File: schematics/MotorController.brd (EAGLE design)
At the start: 160 x 100 mm, 30 parts, among them K1 35701331

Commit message: no message
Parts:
- removed POWER-INPUT: 1, con-lstb:MA03-1
- added DC_MOTOR_DRIVER: SINGLE_MOTOR_DRIVER, pololu motor driver:MOTOR_DRIVER_MC33926_FOOTPRINT_
- added IC1: (no value), v-reg:78XXL
- added LED1: (no value), led:LED3MM
- added LOG-UART: 1, con-lstb:MA03-1
- added POWER_IN: (no value), SparkFun-Connectors:SCREWTERMINAL-3.5MM-2
- added R11: 1K, resistor:0204/5
- D1: value 1N4148DO35-7 -> 1N5400; device diode:DO35-7 -> diode:DO201-15
- MOTOR1, MOTOR2, MOTOR3: value 1 -> 5566-4; device con-lstb:MA03-1 -> con-molex:5566-4
- moved C3 285.2 mm to (44.5, 82.5), turned to 180 degrees
- moved C2 280.7 mm to (124.5, 68.6), turned to 180 degrees
- moved C1 271.8 mm to (116.8, 80.0), turned to 180 degrees
- moved CONTROL-I2C 241.9 mm to (88.9, 86.4), turned to 180 degrees
- moved D1 238.7 mm to (118.1, 53.3)
- moved IMU-I2C 227.0 mm to (63.5, 86.4)
- moved K1 205.4 mm to (138.4, 71.1), turned to 90 degrees
- moved DC-MOTOR 201.4 mm to (127.0, 12.7)
- moved R10 190.6 mm to (100.3, 58.4), turned to 180 degrees
- moved T1 188.1 mm to (106.7, 55.9), turned to 90 degrees
- moved ENCODER1 159.9 mm to (106.7, 12.7), turned to 270 degrees
- moved ENCODER2 159.1 mm to (82.5, 12.7), turned to 270 degrees
- moved R9 155.2 mm to (61.0, 55.9), turned to 270 degrees
- moved R8 151.4 mm to (63.5, 55.9), turned to 270 degrees
- moved R7 147.8 mm to (66.0, 55.9), turned to 270 degrees
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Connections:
- removed net GND: C1.-, C2.-, C3.2, CONTROL-I2C.3, DC-MOTOR.4, DRK1.GND, DRK2.GND, DRK3.GND, ENCODER1.4, ENCODER2.4, ENCODER3.4, IMU-I2C.3, POWER-INPUT.1, PRJ1.GND, T1.1
- removed net VCC: C1.+, C3.1, D1.C, DC-MOTOR.3, ENCODER1.1, ENCODER2.1, ENCODER3.1, K1.3, PRJ1.VIN
- new net BLCK-M2: DC-MOTOR.2, DC_MOTOR_DRIVER.OUT1
- new net ENC_B: DC-MOTOR.6, PRJ1.35/A16
- new net ENC_GND: C1.-, C2.-, C3.2, CONTROL-I2C.3, DC-MOTOR.3, DC_MOTOR_DRIVER.GND, DRK1.GND, DRK2.GND, DRK3.GND, ENCODER1.4, ENCODER2.4, ENCODER3.4, IC1.GND, IMU-I2C.3, LED1.A, LOG-UART.3, POWER_IN.1, PRJ1.GND, T1.1
- new net ENC_VCC: C1.+, C3.1, DC-MOTOR.4, DC_MOTOR_DRIVER.VIN, ENCODER1.1, ENCODER2.1, ENCODER3.1, IC1.OUT, K1.3, PRJ1.VIN, R11.2
- new net N$44: DC_MOTOR_DRIVER.IN1, PRJ1.29
- new net N$45: DC_MOTOR_DRIVER.EN, PRJ1.31/A12
- new net N$46: PRJ1.36/A17
- new net N$47: DC_MOTOR_DRIVER.IN2, PRJ1.30
- new net RED-M1: DC-MOTOR.1, DC_MOTOR_DRIVER.OUT2
- new net RX5: LOG-UART.1, PRJ1.34/A15
- new net TX5: LOG-UART.2, PRJ1.33/A14
- net N$12: now also DC_MOTOR_DRIVER.VIN(5-28V)
- net N$32: now also D1.A, IC1.IN, POWER_IN.2; no longer K1.7, POWER-INPUT.3
- net N$39: now also D1.C, K1.7; no longer D1.A, POWER-INPUT.2
- net N$40: now also LED1.K, R11.1; no longer DC-MOTOR.2, PRJ1.33/A14
- net N$41: now also DC_MOTOR_DRIVER.INV, PRJ1.32/A13; no longer DC-MOTOR.1, PRJ1.34/A15
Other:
- board size 160 x 100 mm -> 130.8 x 100 mm

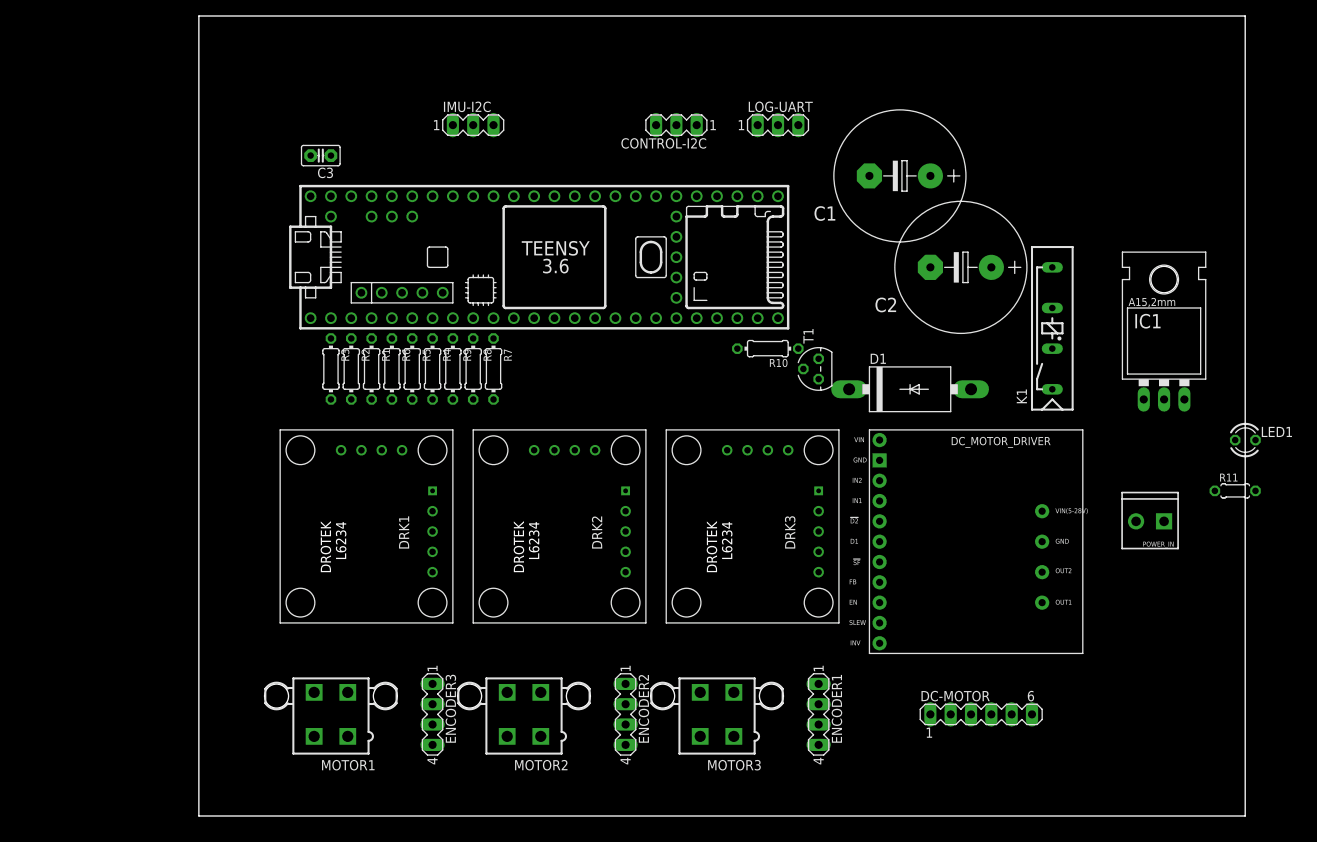
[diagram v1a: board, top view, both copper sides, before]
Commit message: beltdrive wheels got a flange
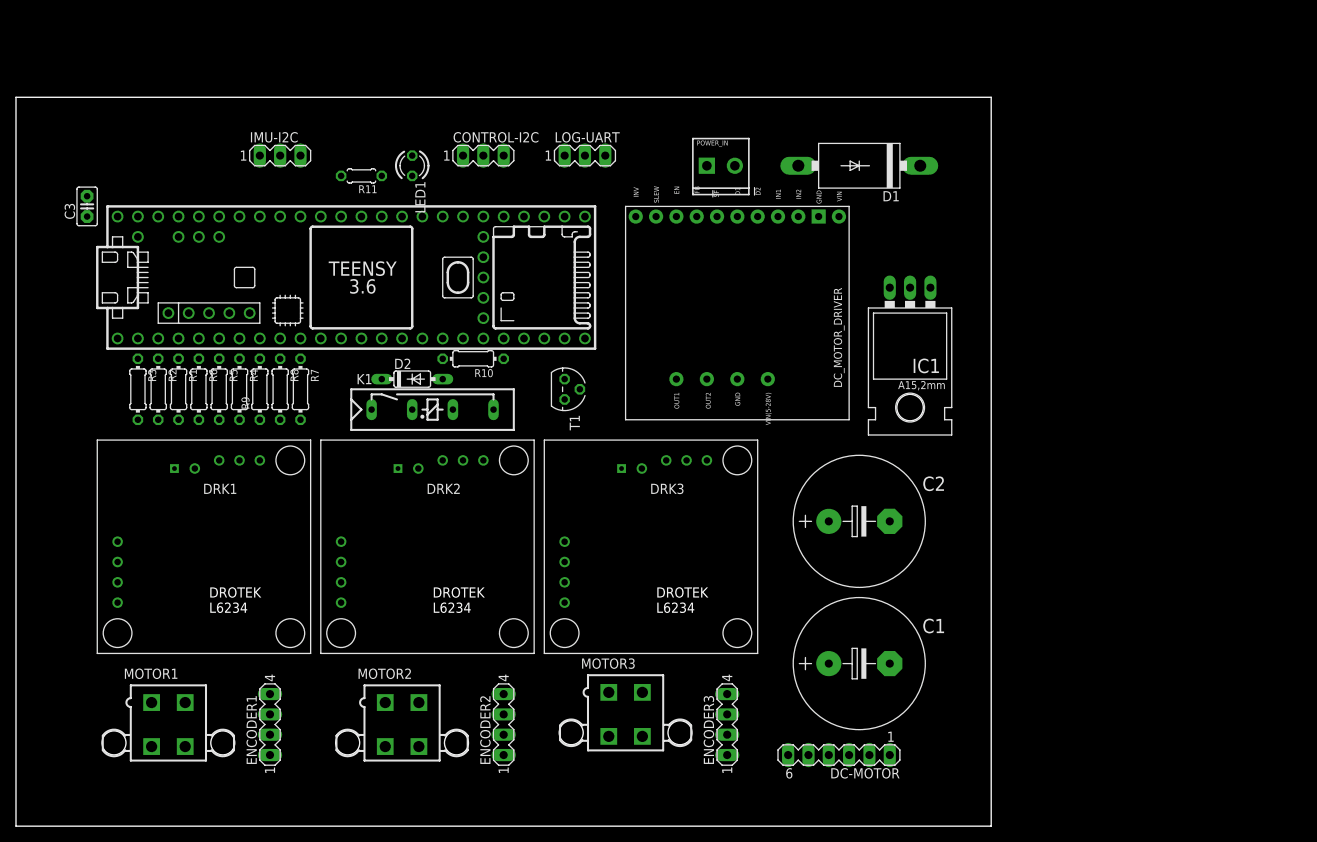
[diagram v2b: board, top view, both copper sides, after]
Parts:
- added D2: 1N4148DO35-7, diode:DO35-7
- C1, C2: value (none) -> 470uF
- C3: value (none) -> 100nF
- IC1: value (none) -> 7805
- LED1: value (none) -> green
- POWER_IN: value (none) -> 12V
- T1: value (none) -> BC338
- moved R11 116.1 mm to (49.5, 80.0), turned to 180 degrees
- moved LED1 109.6 mm to (55.9, 81.3), turned to 270 degrees
- moved K1 73.5 mm to (68.6, 48.3), turned to 0 degrees
- moved POWER_IN 72.4 mm to (92.7, 81.3), turned to 0 degrees
- moved ENCODER1 68.6 mm to (38.1, 11.4), turned to 90 degrees
- moved C1 61.2 mm to (111.8, 19.1), turned to 0 degrees
- moved DC_MOTOR_DRIVER 42.7 mm to (96.5, 71.1), turned to 270 degrees
- moved ENCODER3 36.9 mm to (95.2, 11.4), turned to 90 degrees
- moved R10 36.9 mm to (63.5, 57.1)
- moved C2 34.2 mm to (111.8, 36.8), turned to 0 degrees
- moved IC1 32.4 mm to (118.1, 62.2), turned to 180 degrees
- moved T1 31.9 mm to (74.9, 53.3), turned to 270 degrees
- moved C3 29.9 mm to (15.2, 76.2), turned to 90 degrees
- moved D1 28.7 mm to (111.8, 81.3), turned to 180 degrees
- moved CONTROL-I2C 24.4 mm to (64.8, 82.5), turned to 0 degrees
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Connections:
- net ENC_B renamed WH_ENC_B
- net ENC_GND renamed GND
- removed net ENC_VCC: C1.+, C3.1, DC-MOTOR.4, DC_MOTOR_DRIVER.VIN, ENCODER1.1, ENCODER2.1, ENCODER3.1, IC1.OUT, K1.3, PRJ1.VIN, R11.2
- removed net N$46: PRJ1.36/A17
- new net VCC: C1.+, C3.1, D2.C, DC-MOTOR.4, DC_MOTOR_DRIVER.VIN, ENCODER1.1, ENCODER2.1, ENCODER3.1, IC1.OUT, K1.3, PRJ1.VIN, R11.2
- new net Y_ENC_A: DC-MOTOR.5, PRJ1.36/A17
- net N$31: now also D2.A
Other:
- board size 130.8 x 100 mm -> 121.9 x 91.1 mm

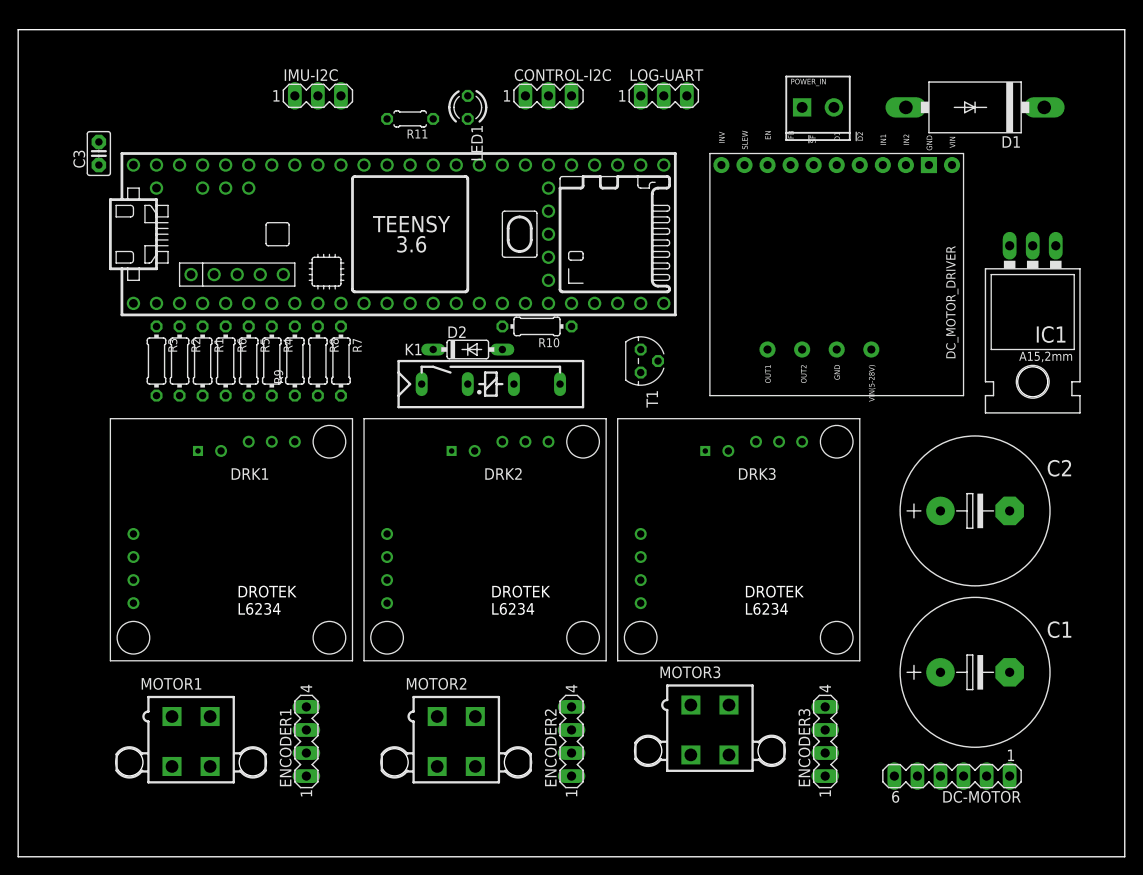
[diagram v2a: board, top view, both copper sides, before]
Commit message: updated drotek and pololu library
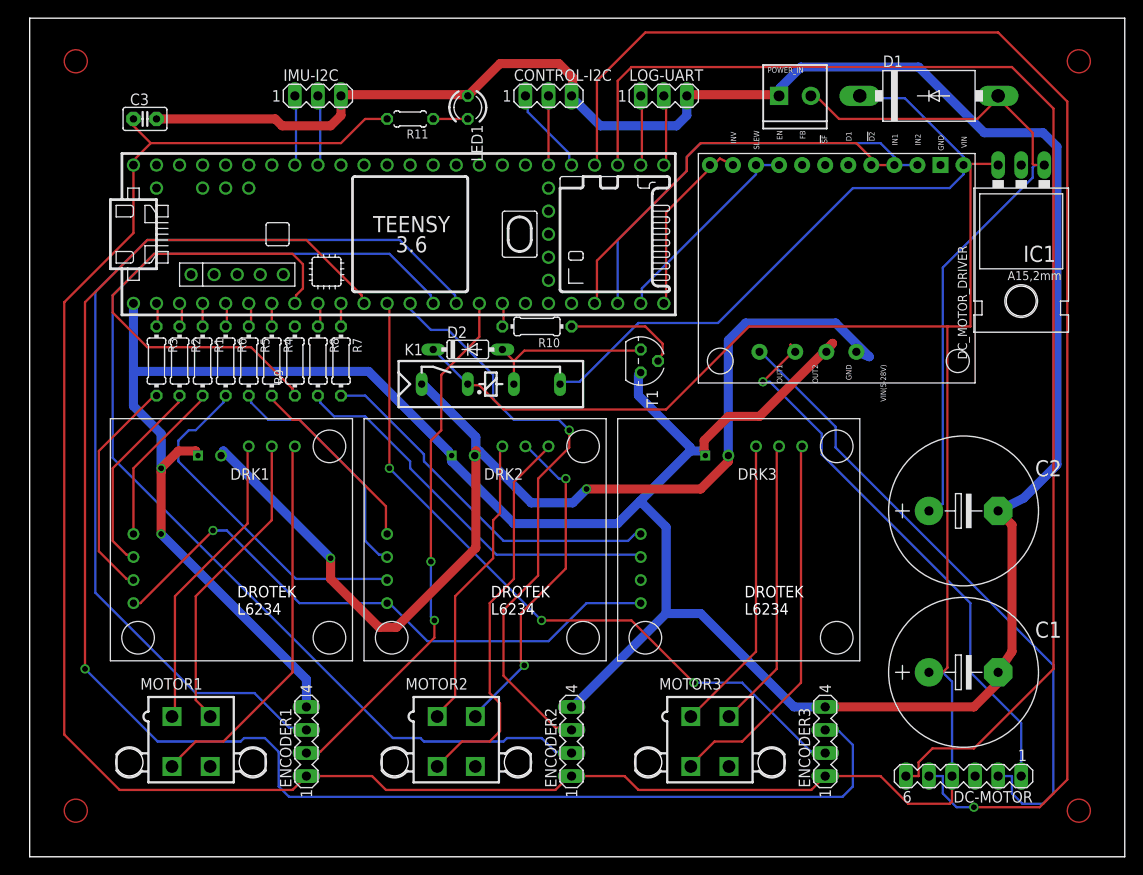
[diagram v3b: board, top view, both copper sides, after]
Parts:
- moved IC1 8.98 mm to (116.8, 71.1)
- moved C3 6.35 mm to (20.3, 80.0), turned to 0 degrees
- moved D1 5.24 mm to (106.7, 82.5), turned to 0 degrees
- moved POWER_IN 2.84 mm to (90.2, 82.5)
- moved C1 1.27 mm to (110.5, 19.1)
- moved C2 1.27 mm to (110.5, 36.8)
- moved DC_MOTOR_DRIVER 1.27 mm to (97.8, 71.1)
- moved MOTOR3 1.27 mm to (82.5, 11.4)
- moved DC-MOTOR 1.27 mm to (110.5, 7.62)
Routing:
- net GND: track 0.00 -> 413.9 mm, vias 0 -> 2
- net VCC: track 0.00 -> 348.0 mm
- net N$33: track 0.00 -> 179.1 mm, vias 0 -> 1
- net Y_ENC_A: track 0.00 -> 160.3 mm, vias 0 -> 1
- net WH_ENC_B: track 0.00 -> 143.6 mm
- net N$12: track 0.00 -> 128.1 mm, vias 0 -> 2
- net N$36: track 0.00 -> 122.1 mm
- net N$37: track 0.00 -> 108.3 mm
- net N$34: track 0.00 -> 79.3 mm, vias 0 -> 3
- net N$32: track 0.00 -> 77.6 mm
- net BLCK-M2: track 0.00 -> 72.4 mm
- net N$39: track 0.00 -> 70.3 mm
- net N$10: track 0.00 -> 66.0 mm, vias 0 -> 1
- net N$35: track 0.00 -> 65.3 mm, vias 0 -> 1
- net RED-M1: track 0.00 -> 62.0 mm, vias 0 -> 1
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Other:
- board size 121.9 x 91.1 mm -> 120.6 x 92.4 mm

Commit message: no message
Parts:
- removed LED1: green, led:LED3MM
- removed R11: 1K, resistor:0204/5
- removed T1: BC338, transistor:TO92
- added Q1: BC307, transistor-pnp:TO92
- added SV1: (no value), con-lstb:MA04-1
- IMU-I2C: device con-lstb:MA03-1 -> con-lstb:MA05-1
- moved ENCODER3 160.3 mm to (-58.4, 57.1), turned to 180 degrees
- moved MOTOR3 141.1 mm to (-58.4, 16.5), turned to 90 degrees
- moved D1 131.4 mm to (-3.81, 11.4)
- moved POWER_IN 130.9 mm to (-11.4, 0.00)
- moved DRK3 127.6 mm to (-39.4, 11.4), turned to 180 degrees
- moved ENCODER2 126.0 mm to (-58.4, 2.54), turned to 180 degrees
- moved MOTOR2 117.4 mm to (-58.4, 43.2), turned to 90 degrees
- moved IC1 104.6 mm to (29.2, 14.0)
- moved MOTOR1 102.9 mm to (-58.4, 71.1), turned to 90 degrees
- moved C2 100.8 mm to (14.0, 7.62), turned to 270 degrees
- moved ENCODER1 98.1 mm to (-58.4, 29.2), turned to 180 degrees
- moved DRK2 98.0 mm to (-39.4, 39.4), turned to 180 degrees
- moved C1 92.0 mm to (19.1, 29.2), turned to 270 degrees
- moved DC-MOTOR 90.7 mm to (45.7, 71.1), turned to 270 degrees
- moved D2 87.5 mm to (-22.9, 16.5), turned to 90 degrees
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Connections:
- removed net N$40: LED1.K, R11.1
- new net N$46: IMU-I2C.4, PRJ1.3V3_LO
- new net N$48: IMU-I2C.1, PRJ1.20/A6
- new net N$49: PRJ1.23/A9, SV1.1
- new net N$50: PRJ1.22/A8, SV1.2
- new net N$51: PRJ1.21/A7, SV1.3
- net GND: now also D2.A, IMU-I2C.5, K1.5, SV1.4; no longer IMU-I2C.3, LED1.A, T1.1
- net IMU-SCL: now also IMU-I2C.2; no longer IMU-I2C.1
- net IMU-SDA: now also IMU-I2C.3; no longer IMU-I2C.2
- net N$30: now also Q1.2; no longer T1.2
- net N$31: now also D2.C, K1.3, Q1.3; no longer D2.A, K1.5, T1.3
- net VCC: now also Q1.1; no longer D2.C, K1.3, R11.2
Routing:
- net N$45: track 22.9 -> 159.8 mm
- net N$33: track 179.1 -> 50.8 mm
- net N$44: track 44.9 -> 169.5 mm
- net N$41: track 20.2 -> 130.4 mm, vias 0 -> 1
- net N$49: track 0.00 -> 87.6 mm
- net Y_ENC_A: track 160.3 -> 73.8 mm, vias 1 -> 3
- net N$51: track 0.00 -> 83.5 mm, vias 0 -> 1
- net WH_ENC_B: track 143.6 -> 66.8 mm, vias 0 -> 2
- net N$46: track 0.00 -> 72.8 mm, vias 0 -> 1
- net N$50: track 0.00 -> 62.8 mm, vias 0 -> 2
- net GND: track 413.9 -> 474.3 mm
- net CTRL-SDA: track 9.78 -> 68.5 mm
- net N$48: track 0.00 -> 56.2 mm
- net IMU-SDA: track 7.88 -> 63.7 mm, vias 0 -> 2
- net N$43: track 7.62 -> 63.2 mm
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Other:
- board size 120.6 x 92.4 mm -> 132.1 x 98.7 mm

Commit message: no message
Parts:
- removed K1: 35701331, relay:REED
- added R11: 0, resistor:0204V
- added REL1: HF49FD, relay:HF49FD
- added S1: (no value), switch-dil:DA-02
- moved D2 15.3 mm to (-7.62, 15.2), turned to 0 degrees
- moved C1 10.9 mm to (29.2, 33.0), turned to 90 degrees
- moved IC1 8.98 mm to (30.5, 5.08), turned to 0 degrees
- moved IMU-I2C 4.02 mm to (44.5, 35.6)
- moved SV1 2.84 mm to (44.5, 53.3)
- moved D1 2.84 mm to (-5.08, 8.89)
- moved POWER_IN 2.84 mm to (-8.89, 1.27)
- moved C2 2.54 mm to (14.0, 5.08)
- moved DC-MOTOR 1.80 mm to (44.5, 72.4), turned to 90 degrees
- moved CONTROL-I2C 1.27 mm to (44.5, 3.81)
- moved LOG-UART 1.27 mm to (44.5, 19.1)
- renumbered DC_MOTOR_DRIVER to U$1
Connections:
- new net LIPO-GND: DRK1.GND, DRK2.GND, DRK3.GND, POWER_IN.1, R11.1, U$1.GND
- new net LIPO-VDD: DRK1.LIPO+, DRK2.LIPO+, DRK3.LIPO+, REL1.3, U$1.VIN(5-28V)
- new net N$40: PRJ1.39/A20, S1.4
- net BLCK-M2: now also U$1.OUT2; no longer U$1.OUT1
- net GND: now also R11.2, REL1.2, S1.1, S1.2; no longer DRK1.GND, DRK2.GND, DRK3.GND, K1.5, POWER_IN.1, U$1.GND
- net N$12: now also PRJ1.21/DAC0, S1.3; no longer DRK1.LIPO+, DRK2.LIPO+, DRK3.LIPO+, K1.1, U$1.VIN(5-28V)
- net N$31: now also REL1.1; no longer K1.3
- net N$39: now also REL1.4; no longer K1.7
- net N$41: now also U$1.VDD; no longer U$1.INV
- net RED-M1: now also U$1.OUT1; no longer U$1.OUT2
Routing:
- net GND: track 474.3 -> 0.00 mm, vias 2 -> 0
- net VCC: track 308.2 -> 0.00 mm, vias 3 -> 0
- net N$12: track 178.0 -> 0.00 mm, vias 3 -> 0
- net N$44: track 169.5 -> 0.00 mm
- net N$45: track 159.8 -> 0.00 mm
- net N$41: track 130.4 -> 0.00 mm, vias 1 -> 0
- net N$47: track 97.5 -> 0.00 mm, vias 4 -> 0
- net N$36: track 87.9 -> 0.00 mm, vias 1 -> 0
- net N$49: track 87.6 -> 0.00 mm
- net N$51: track 83.5 -> 0.00 mm, vias 1 -> 0
- net N$35: track 80.1 -> 0.00 mm, vias 1 -> 0
- net Y_ENC_A: track 73.8 -> 0.00 mm, vias 3 -> 0
- net N$46: track 72.8 -> 0.00 mm, vias 1 -> 0
- net N$37: track 71.9 -> 0.00 mm, vias 2 -> 0
- net N$38: track 69.2 -> 0.00 mm, vias 1 -> 0
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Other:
- board size 132.1 x 98.7 mm -> 127 x 96.2 mm

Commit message: no message
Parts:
- moved CONTROL-I2C 3.81 mm to (40.6, 3.81)
- moved DC-MOTOR 3.81 mm to (40.6, 72.4)
- moved IMU-I2C 3.81 mm to (40.6, 35.6)
- moved LOG-UART 3.81 mm to (40.6, 19.1)
- moved SV1 3.81 mm to (40.6, 53.3)
- moved U$1 3.81 mm to (14.0, 64.8)
- moved C2 2.84 mm to (12.7, 7.62)
- moved IC1 2.54 mm to (27.9, 5.08)
- moved C1 1.27 mm to (27.9, 33.0)
- moved R1 1.27 mm to (-19.1, 69.8)
- moved R2 1.27 mm to (-19.1, 72.4)
- moved R3 1.27 mm to (-19.1, 74.9)
- moved R4 1.27 mm to (-19.1, 62.2)
- moved R5 1.27 mm to (-19.1, 64.8)
- moved R6 1.27 mm to (-19.1, 67.3)
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
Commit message: no message
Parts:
- moved ENCODER3 55.9 mm to (-58.4, 1.27)
- moved ENCODER1 27.9 mm to (-58.4, 57.1)
- moved ENCODER2 26.7 mm to (-58.4, 29.2)
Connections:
- net N$10: now also PRJ1.24
- net N$21: now also PRJ1.5; no longer PRJ1.3/CANTX
- net N$22: now also PRJ1.6; no longer PRJ1.4/CANRX
- net N$23: now also PRJ1.7; no longer PRJ1.5
- net N$27: now also PRJ1.8; no longer PRJ1.6
- net N$28: now also PRJ1.9/CS; no longer PRJ1.7
- net N$29: now also PRJ1.10/CS; no longer PRJ1.8
- net N$33: now also ENCODER1.3, PRJ1.11/MOSI; no longer ENCODER3.3, PRJ1.9/CS
- net N$34: now also ENCODER1.2, PRJ1.12/MISO; no longer ENCODER3.2, PRJ1.10/CS
- net N$35: now also PRJ1.25; no longer PRJ1.11/MOSI
- net N$36: now also PRJ1.26; no longer PRJ1.12/MISO
- net N$37: now also ENCODER3.3, PRJ1.27; no longer ENCODER1.3, PRJ1.3V3
- net N$38: now also ENCODER3.2, PRJ1.28; no longer ENCODER1.2, PRJ1.24
- net N$42: no longer PRJ1.25
- net N$7: now also PRJ1.4/CANRX; no longer PRJ1.2
- net N$8: now also PRJ1.3/CANTX; no longer PRJ1.1/TX
- net N$9: now also PRJ1.2; no longer PRJ1.0/RX
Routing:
- net GND: track 0.00 -> 368.9 mm
- net VCC: track 0.00 -> 353.1 mm, vias 0 -> 3
- net LIPO-GND: track 0.00 -> 206.0 mm, vias 0 -> 1
- net LIPO-VDD: track 0.00 -> 170.2 mm, vias 0 -> 4
- net N$41: track 0.00 -> 108.0 mm, vias 0 -> 1
- net N$44: track 0.00 -> 98.5 mm, vias 0 -> 2
- net WH_ENC_B: track 0.00 -> 93.9 mm, vias 0 -> 1
- net N$46: track 0.00 -> 91.4 mm
- net N$33: track 0.00 -> 89.9 mm
- net Y_ENC_A: track 0.00 -> 88.6 mm, vias 0 -> 1
- net N$48: track 0.00 -> 88.1 mm, vias 0 -> 1
- net N$34: track 0.00 -> 87.0 mm
- net N$47: track 0.00 -> 85.2 mm, vias 0 -> 2
- net N$36: track 0.00 -> 81.9 mm
- net N$10: track 0.00 -> 75.0 mm, vias 0 -> 1
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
